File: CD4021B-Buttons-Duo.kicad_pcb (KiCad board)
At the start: 2 copper layers, 100 x 50 mm, 49 parts, among them J1 2.54, J10 JST XH, J11 JST XH, J12 JST XH, J13 JST XH, J14 JST XH, J15 JST XH, J16 JST XH, J17 JST XH, J2 JST XH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

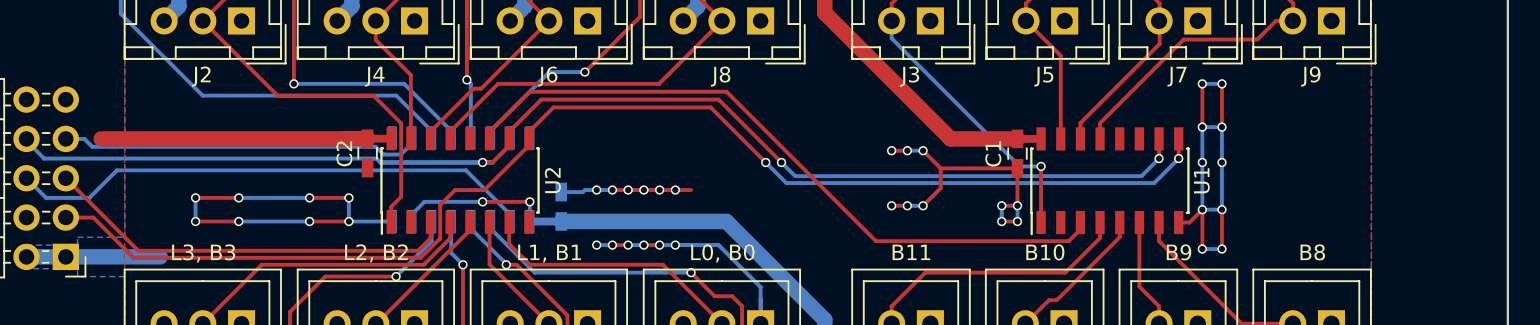
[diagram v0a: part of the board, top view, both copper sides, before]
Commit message: Add screw terminal to the board for lamp power
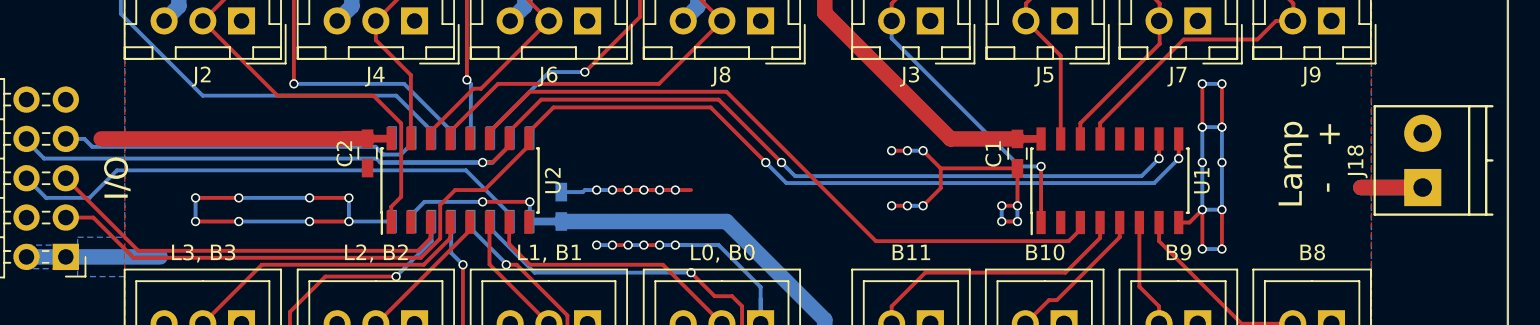
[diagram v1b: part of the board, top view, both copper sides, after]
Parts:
- added J18: 3.5, TerminalBlocks_Phoenix:TerminalBlock_Phoenix_PT-3.5mm_2pol, F.Cu at (199.9, 105.0)
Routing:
- net GND: track 111.2 -> 119.2 mm
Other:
- board text added: "+"
- board text added: "-"
- board text added: "I/O"
- board text added: "Lamp"
- board text added: "V1.3.0"
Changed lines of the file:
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@@
 (kicad_pcb (version 4) (host pcbnew 4.0.7)
   (general
-    (links 153)
+    (links 155)
     (no_connects 0)
     (area 105.334999 78.918999 205.485001 129.069001)
     (thickness 1.6)
-    (drawings 23)
-    (tracks 431)
+    (drawings 28)
+    (tracks 433)
     (zones 0)
-    (modules 49)
+    (modules 50)
     (nets 48)
   )
@@
     (title "CD4021B Buttons Duo")
     (date 2018-05-16)
-    (rev 1.2.0)
+    (rev 1.3.0)
   )
   (layers
@@
       (xy -2.537313 2.939947) (xy -2.454562 2.96715) (xy -2.376928 2.977424) (xy -2.273043 2.973429)) (layer B.SilkS) (width 0.01))
   )
+  (module TerminalBlocks_Phoenix:TerminalBlock_Phoenix_PT-3.5mm_2pol (layer F.Cu)
+    (at 199.91 104.994 90)
+    (descr "2-way 3.5mm pitch terminal block, Phoenix PT series")
+    (fp_text reference J18 (at 1.75 -4.3 90) (layer F.SilkS)
+      (effects (font (size 1 1) (thickness 0.15)))
+    )
+    (fp_text value 3.5 (at 1.75 6 90) (layer F.Fab)
+      (effects (font (size 1 1) (thickness 0.15)))
+    )
+    (fp_text user %R (at 1.75 0 90) (layer F.Fab)
+      (effects (font (size 1 1) (thickness 0.15)))
+    )
+    (fp_line (start -1.9 -3.3) (end 5.4 -3.3) (layer F.CrtYd) (width 0.05))
+    (fp_line (start -1.9 4.7) (end -1.9 -3.3) (layer F.CrtYd) (width 0.05))
+    (fp_line (start 5.4 4.7) (end -1.9 4.7) (layer F.CrtYd) (width 0.05))
+    (fp_line (start 5.4 -3.3) (end 5.4 4.7) (layer F.CrtYd) (width 0.05))
+    (fp_line (start 1.75 4.1) (end 1.75 4.5) (layer F.SilkS) (width 0.15))
+    (fp_line (start -1.75 3) (end 5.25 3) (layer F.SilkS) (width 0.15))
+    (fp_line (start -1.75 4.1) (end 5.25 4.1) (layer F.SilkS) (width 0.15))
+    (fp_line (start -1.75 -3.1) (end -1.75 4.5) (layer F.SilkS) (width 0.15))
+    (fp_line (start 5.25 4.5) (end 5.25 -3.1) (layer F.SilkS) (width 0.15))
+    (fp_line (start 5.25 -3.1) (end -1.75 -3.1) (layer F.SilkS) (width 0.15))
+    (pad 2 thru_hole circle (at 3.5 0 90) (size 2.4 2.4) (drill 1.2) (layers *.Cu *.Mask)
+      (net 3 +12V))
+    (pad 1 thru_hole rect (at 0 0 90) (size 2.4 2.4) (drill 1.2) (layers *.Cu *.Mask)
+      (net 2 GND))
+    (model ${KISYS3DMOD}/TerminalBlock_Phoenix.3dshapes/TerminalBlock_Phoenix_PT-3.5mm_2pol.wrl
+      (at (xyz 0 0 0))
+      (scale (xyz 1 1 1))
+      (rotate (xyz 0 0 0))
+    )
+  )
+  (gr_text V1.3.0 (at 110.998 116.078) (layer B.SilkS)
+    (effects (font (size 1.5 1.5) (thickness 0.3)) (justify mirror))
+  )
+  (gr_text + (at 193.91 101.494) (layer F.SilkS)
+    (effects (font (size 1.5 1.5) (thickness 0.3)))
+  )
+  (gr_text - (at 193.675 104.994 90) (layer F.SilkS)
+    (effects (font (size 1.5 1.5) (thickness 0.3)))
+  )
+  (gr_text I/O (at 115.57 104.394 90) (layer F.SilkS)
+    (effects (font (size 1.5 1.5) (thickness 0.3)))
+  )
+  (gr_text Lamp (at 191.41 103.494 90) (layer F.SilkS)
+    (effects (font (size 1.5 1.5) (thickness 0.3)))
+  )
   (gr_text B8 (at 192.786 109.22) (layer F.SilkS)
     (effects (font (size 1 1) (thickness 0.15)))
@@
   (segment (start 131.760454 101.838502) (end 130.385454 101.838502) (width 1) (layer F.Cu) (net 1) (status 10))
   (segment (start 130.385454 101.838502) (end 130.369956 101.854) (width 1) (layer F.Cu) (net 1))
+  (segment (start 199.91 104.994) (end 195.91 104.994) (width 1) (layer B.Cu) (net 2))
+  (segment (start 199.91 104.994) (end 195.91 104.994) (width 1) (layer F.Cu) (net 2))
   (segment (start 123.444 107.188) (end 128.016 107.188) (width 0.25) (layer B.Cu) (net 2))
   (segment (start 130.556 107.188) (end 128.016 107.188) (width 0.25) (layer F.Cu) (net 2))

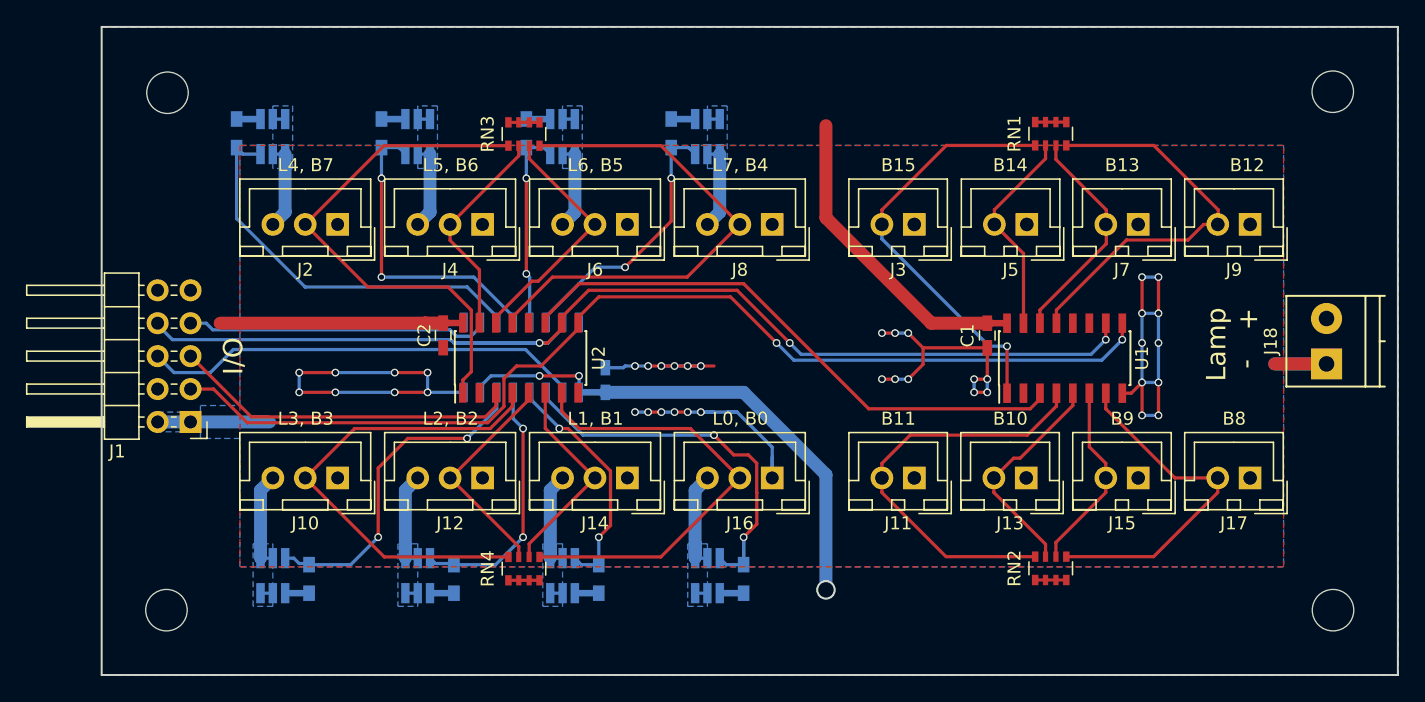
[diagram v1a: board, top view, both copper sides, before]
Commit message: Re-routed using vertical-horizontal routing rule
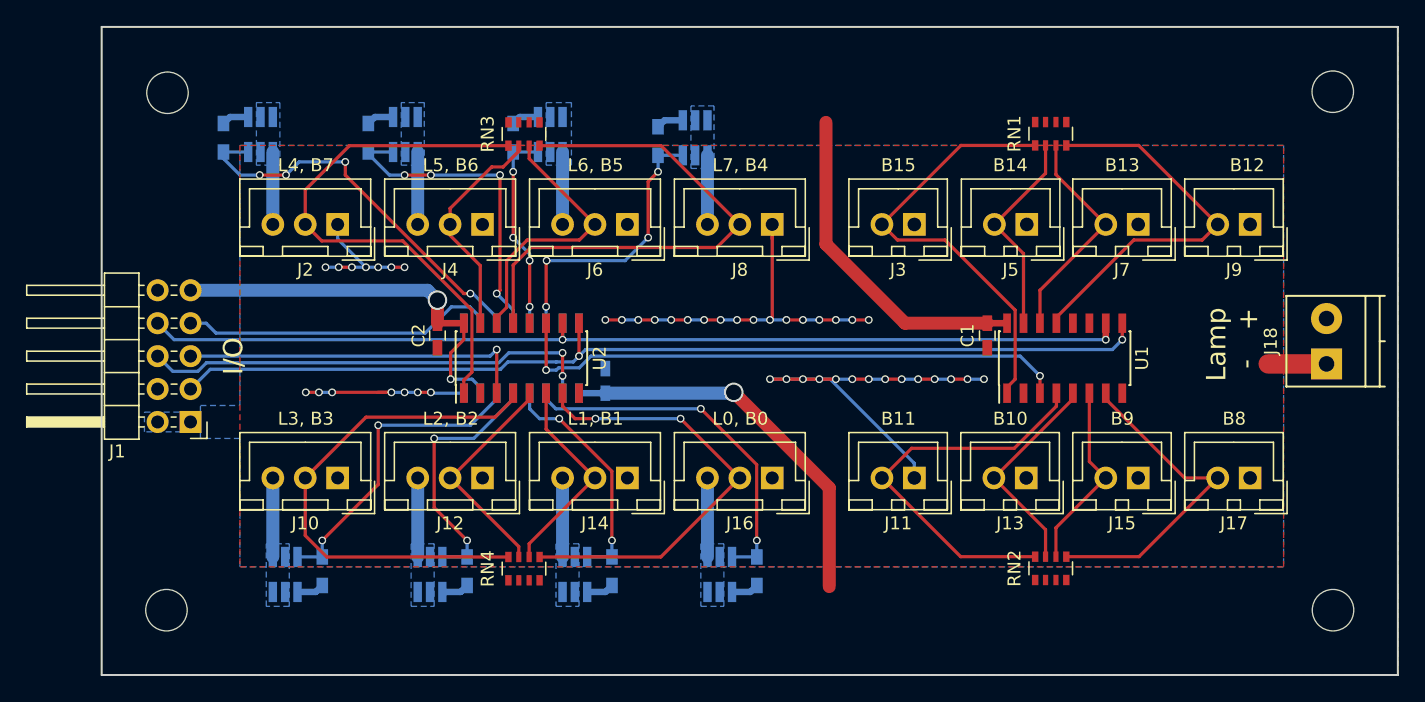
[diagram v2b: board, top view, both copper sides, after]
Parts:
- moved R5 1.18 mm to (133.6, 121.0)
- moved R1 1.18 mm to (156.0, 121.0)
- moved R2 1.18 mm to (148.3, 87.8)
- moved R3 1.18 mm to (144.8, 121.0)
- moved R7 1.18 mm to (122.4, 121.0)
- moved R6 1.07 mm to (126.0, 87.5)
- moved R4 1.07 mm to (137.2, 87.5)
- moved R8 1.07 mm to (114.8, 87.5)
- moved Q6 0.96 mm to (128.8, 87.3)
- moved Q4 0.96 mm to (140.0, 87.3)
- moved Q8 0.96 mm to (117.7, 87.3)
- moved Q1 0.95 mm to (153.1, 121.2)
- moved Q7 0.95 mm to (119.6, 121.2)
- moved Q2 0.95 mm to (151.2, 87.5)
- moved Q3 0.95 mm to (141.9, 121.2)
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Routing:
- net GND: track 119.2 -> 88.4 mm, vias 40 -> 45
- net /SCK: track 89.8 -> 77.5 mm, vias 3 -> 2
- net VCC: track 93.0 -> 86.8 mm
- net /CSI: track 82.7 -> 77.3 mm
- net /L0: track 9.50 -> 6.10 mm
- net /L2: track 9.25 -> 6.10 mm
- net /L1: track 9.25 -> 6.10 mm
- net /LD0: track 30.6 -> 27.8 mm
- net /L4: track 7.72 -> 5.33 mm
- net /L3: track 8.48 -> 6.10 mm
- net /D3: track 37.5 -> 39.8 mm
- net /D4: track 38.9 -> 41.2 mm
- net +12V: track 14.8 -> 16.9 mm
- net /L7: track 7.72 -> 5.59 mm
- net /L6: track 7.72 -> 5.59 mm
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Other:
- board text added: "V1.4.0"
- board text removed: "V1.3.0"

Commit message: Minor adjustment
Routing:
- net /LD3: track 24.3 -> 23.7 mm
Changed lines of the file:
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@@
     (links 155)
     (no_connects 0)
-    (area 97.329048 78.918999 213.490953 129.069001)
+    (area 105.334999 78.918999 205.485001 129.069001)
     (thickness 1.6)
     (drawings 28)
-    (tracks 396)
+    (tracks 399)
     (zones 0)
     (modules 50)
@@
   (segment (start 125.984 88.796) (end 125.984 88.646) (width 0.25) (layer B.Cu) (net 38) (status 30))
   (segment (start 125.984 88.646) (end 127.894 88.646) (width 0.25) (layer B.Cu) (net 38) (status 30))
+  (segment (start 127.508 109.982) (end 127.045999 110.444001) (width 0.25) (layer B.Cu) (net 39))
+  (segment (start 133.612 109.982) (end 127.508 109.982) (width 0.25) (layer B.Cu) (net 39))
+  (segment (start 135.89 107.704) (end 133.612 109.982) (width 0.25) (layer B.Cu) (net 39))
+  (segment (start 135.89 107.254) (end 135.89 107.704) (width 0.25) (layer B.Cu) (net 39))
+  (segment (start 126.746 111.168264) (end 126.746 110.744) (width 0.25) (layer F.Cu) (net 39))
+  (segment (start 122.428 118.618) (end 126.746 114.3) (width 0.25) (layer F.Cu) (net 39))
+  (segment (start 127.045999 110.444001) (end 126.746 110.744) (width 0.25) (layer B.Cu) (net 39))
+  (segment (start 126.746 114.3) (end 126.746 111.168264) (width 0.25) (layer F.Cu) (net 39))
+  (via (at 126.746 110.744) (size 0.6) (drill 0.4) (layers F.Cu B.Cu) (net 39))
   (segment (start 122.428 119.888) (end 120.518 119.888) (width 0.25) (layer B.Cu) (net 39) (status 30))
   (segment (start 122.428 118.618) (end 122.428 119.888) (width 0.25) (layer B.Cu) (net 39) (status 20))
-  (segment (start 126.746 114.3) (end 122.428 118.618) (width 0.25) (layer F.Cu) (net 39))
-  (segment (start 126.746 109.728) (end 126.746 114.3) (width 0.25) (layer F.Cu) (net 39))
   (via (at 122.428 118.618) (size 0.6) (drill 0.4) (layers F.Cu B.Cu) (net 39))
-  (segment (start 133.866 109.728) (end 126.746 109.728) (width 0.25) (layer B.Cu) (net 39))
-  (segment (start 135.89 107.704) (end 133.866 109.728) (width 0.25) (layer B.Cu) (net 39) (status 10))
-  (segment (start 135.89 107.254) (end 135.89 107.704) (width 0.25) (layer B.Cu) (net 39) (status 30))
-  (via (at 126.746 109.728) (size 0.6) (drill 0.4) (layers F.Cu B.Cu) (net 39))
   (segment (start 135.89 101.404) (end 134.054 99.568) (width 0.25) (layer B.Cu) (net 40) (status 10))
   (segment (start 135.89 101.854) (end 135.89 101.404) (width 0.25) (layer B.Cu) (net 40) (status 30))

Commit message: Minor cleanup
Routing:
- net /LD7: track 30.5 -> 32.8 mm
- net /D7: track 42.0 -> 43.3 mm
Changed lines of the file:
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@@
     (links 155)
     (no_connects 0)
-    (area 105.334999 78.918999 205.485001 129.069001)
+    (area 97.329048 78.918999 213.490953 129.069001)
     (thickness 1.6)
     (drawings 28)
-    (tracks 399)
+    (tracks 400)
     (zones 0)
     (modules 50)
@@
   (segment (start 133.35 107.254) (end 133.35 106.254) (width 0.25) (layer F.Cu) (net 10) (status 10))
   (segment (start 133.35 106.254) (end 133.975001 105.628999) (width 0.25) (layer F.Cu) (net 10))
+  (segment (start 122.896 96.012) (end 121.118 94.234) (width 0.25) (layer F.Cu) (net 10) (status 20))
   (segment (start 133.975001 105.628999) (end 133.975001 100.843999) (width 0.25) (layer F.Cu) (net 10))
-  (segment (start 133.975001 100.843999) (end 128.635002 95.504) (width 0.25) (layer F.Cu) (net 10))
-  (segment (start 128.635002 95.504) (end 122.388 95.504) (width 0.25) (layer F.Cu) (net 10))
-  (segment (start 122.388 95.504) (end 121.118 94.234) (width 0.25) (layer F.Cu) (net 10) (status 20))
+  (segment (start 133.975001 100.843999) (end 133.096 99.964998) (width 0.25) (layer F.Cu) (net 10))
+  (segment (start 133.096 99.964998) (end 133.096 97.79) (width 0.25) (layer F.Cu) (net 10))
+  (segment (start 133.096 97.79) (end 131.318 96.012) (width 0.25) (layer F.Cu) (net 10))
+  (segment (start 131.318 96.012) (end 122.896 96.012) (width 0.25) (layer F.Cu) (net 10))
   (segment (start 136.792 88.16) (end 124.528998 88.16) (width 0.25) (layer F.Cu) (net 10) (status 10))
   (segment (start 124.528998 88.16) (end 121.118 91.570998) (width 0.25) (layer F.Cu) (net 10))
@@
   (via (at 151.638 108.458) (size 0.6) (drill 0.4) (layers F.Cu B.Cu) (net 33))
   (segment (start 154.046 119.888) (end 155.956 119.888) (width 0.25) (layer B.Cu) (net 33) (status 30))
-  (segment (start 147.574 90.932006) (end 147.574 95.25) (width 0.25) (layer F.Cu) (net 34))
-  (segment (start 148.336 90.170006) (end 147.574 90.932006) (width 0.25) (layer F.Cu) (net 34))
-  (segment (start 145.796 97.028) (end 147.574 95.25) (width 0.25) (layer B.Cu) (net 34))
-  (segment (start 139.738013 97.028) (end 145.796 97.028) (width 0.25) (layer B.Cu) (net 34))
-  (via (at 147.574 95.25) (size 0.6) (drill 0.4) (layers F.Cu B.Cu) (net 34))
+  (segment (start 146.558 97.028) (end 148.336 95.25) (width 0.25) (layer B.Cu) (net 34))
+  (segment (start 139.738013 97.028) (end 146.558 97.028) (width 0.25) (layer B.Cu) (net 34))
+  (segment (start 148.336 90.170006) (end 148.336 95.25) (width 0.25) (layer F.Cu) (net 34))
+  (via (at 148.336 95.25) (size 0.6) (drill 0.4) (layers F.Cu B.Cu) (net 34))
   (segment (start 139.7 97.066013) (end 139.738013 97.028) (width 0.25) (layer F.Cu) (net 34))
   (segment (start 139.7 100.584) (end 139.7 97.066013) (width 0.25) (layer F.Cu) (net 34))
@@
   (segment (start 125.984 88.796) (end 125.984 88.646) (width 0.25) (layer B.Cu) (net 38) (status 30))
   (segment (start 125.984 88.646) (end 127.894 88.646) (width 0.25) (layer B.Cu) (net 38) (status 30))
-  (segment (start 127.508 109.982) (end 127.045999 110.444001) (width 0.25) (layer B.Cu) (net 39))
+  (segment (start 127.508 109.982) (end 126.746 110.744) (width 0.25) (layer B.Cu) (net 39))
   (segment (start 133.612 109.982) (end 127.508 109.982) (width 0.25) (layer B.Cu) (net 39))
-  (segment (start 135.89 107.704) (end 133.612 109.982) (width 0.25) (layer B.Cu) (net 39))
-  (segment (start 135.89 107.254) (end 135.89 107.704) (width 0.25) (layer B.Cu) (net 39))
-  (segment (start 126.746 111.168264) (end 126.746 110.744) (width 0.25) (layer F.Cu) (net 39))
+  (segment (start 135.89 107.704) (end 133.612 109.982) (width 0.25) (layer B.Cu) (net 39) (status 10))
+  (segment (start 135.89 107.254) (end 135.89 107.704) (width 0.25) (layer B.Cu) (net 39) (status 30))
+  (segment (start 126.746 114.3) (end 126.746 110.744) (width 0.25) (layer F.Cu) (net 39))
   (segment (start 122.428 118.618) (end 126.746 114.3) (width 0.25) (layer F.Cu) (net 39))
-  (segment (start 127.045999 110.444001) (end 126.746 110.744) (width 0.25) (layer B.Cu) (net 39))
-  (segment (start 126.746 114.3) (end 126.746 111.168264) (width 0.25) (layer F.Cu) (net 39))
   (via (at 126.746 110.744) (size 0.6) (drill 0.4) (layers F.Cu B.Cu) (net 39))
   (segment (start 122.428 119.888) (end 120.518 119.888) (width 0.25) (layer B.Cu) (net 39) (status 30))
   (segment (start 122.428 118.618) (end 122.428 119.888) (width 0.25) (layer B.Cu) (net 39) (status 20))
   (via (at 122.428 118.618) (size 0.6) (drill 0.4) (layers F.Cu B.Cu) (net 39))
+  (segment (start 124.206 89.408) (end 124.206 92.456) (width 0.25) (layer F.Cu) (net 40))
+  (segment (start 131.826 95.504) (end 133.858 97.536) (width 0.25) (layer F.Cu) (net 40))
+  (segment (start 124.206 92.456) (end 127.254 95.504) (width 0.25) (layer F.Cu) (net 40))
+  (segment (start 127.254 95.504) (end 131.826 95.504) (width 0.25) (layer F.Cu) (net 40))
+  (segment (start 133.858 97.536) (end 133.858 99.568) (width 0.25) (layer F.Cu) (net 40))
+  (segment (start 134.054 99.568) (end 133.858 99.568) (width 0.25) (layer B.Cu) (net 40))
   (segment (start 135.89 101.404) (end 134.054 99.568) (width 0.25) (layer B.Cu) (net 40) (status 10))
   (segment (start 135.89 101.854) (end 135.89 101.404) (width 0.25) (layer B.Cu) (net 40) (status 30))
-  (segment (start 133.351998 99.568) (end 133.858 99.568) (width 0.25) (layer F.Cu) (net 40))
-  (segment (start 124.206 89.408) (end 124.206 90.422002) (width 0.25) (layer F.Cu) (net 40))
-  (segment (start 124.206 90.422002) (end 133.351998 99.568) (width 0.25) (layer F.Cu) (net 40))
-  (segment (start 134.054 99.568) (end 133.858 99.568) (width 0.25) (layer B.Cu) (net 40))
   (via (at 133.858 99.568) (size 0.6) (drill 0.4) (layers F.Cu B.Cu) (net 40))
   (segment (start 114.808 88.646) (end 114.808 89.154) (width 0.25) (layer B.Cu) (net 40) (status 30))
